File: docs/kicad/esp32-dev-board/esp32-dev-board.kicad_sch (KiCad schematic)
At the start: 6 parts, among them K1 2-Ch Relay Module, U1 ESP32 Dev Board, U2 DS18B20 Solar, U3 DS18B20 Pool

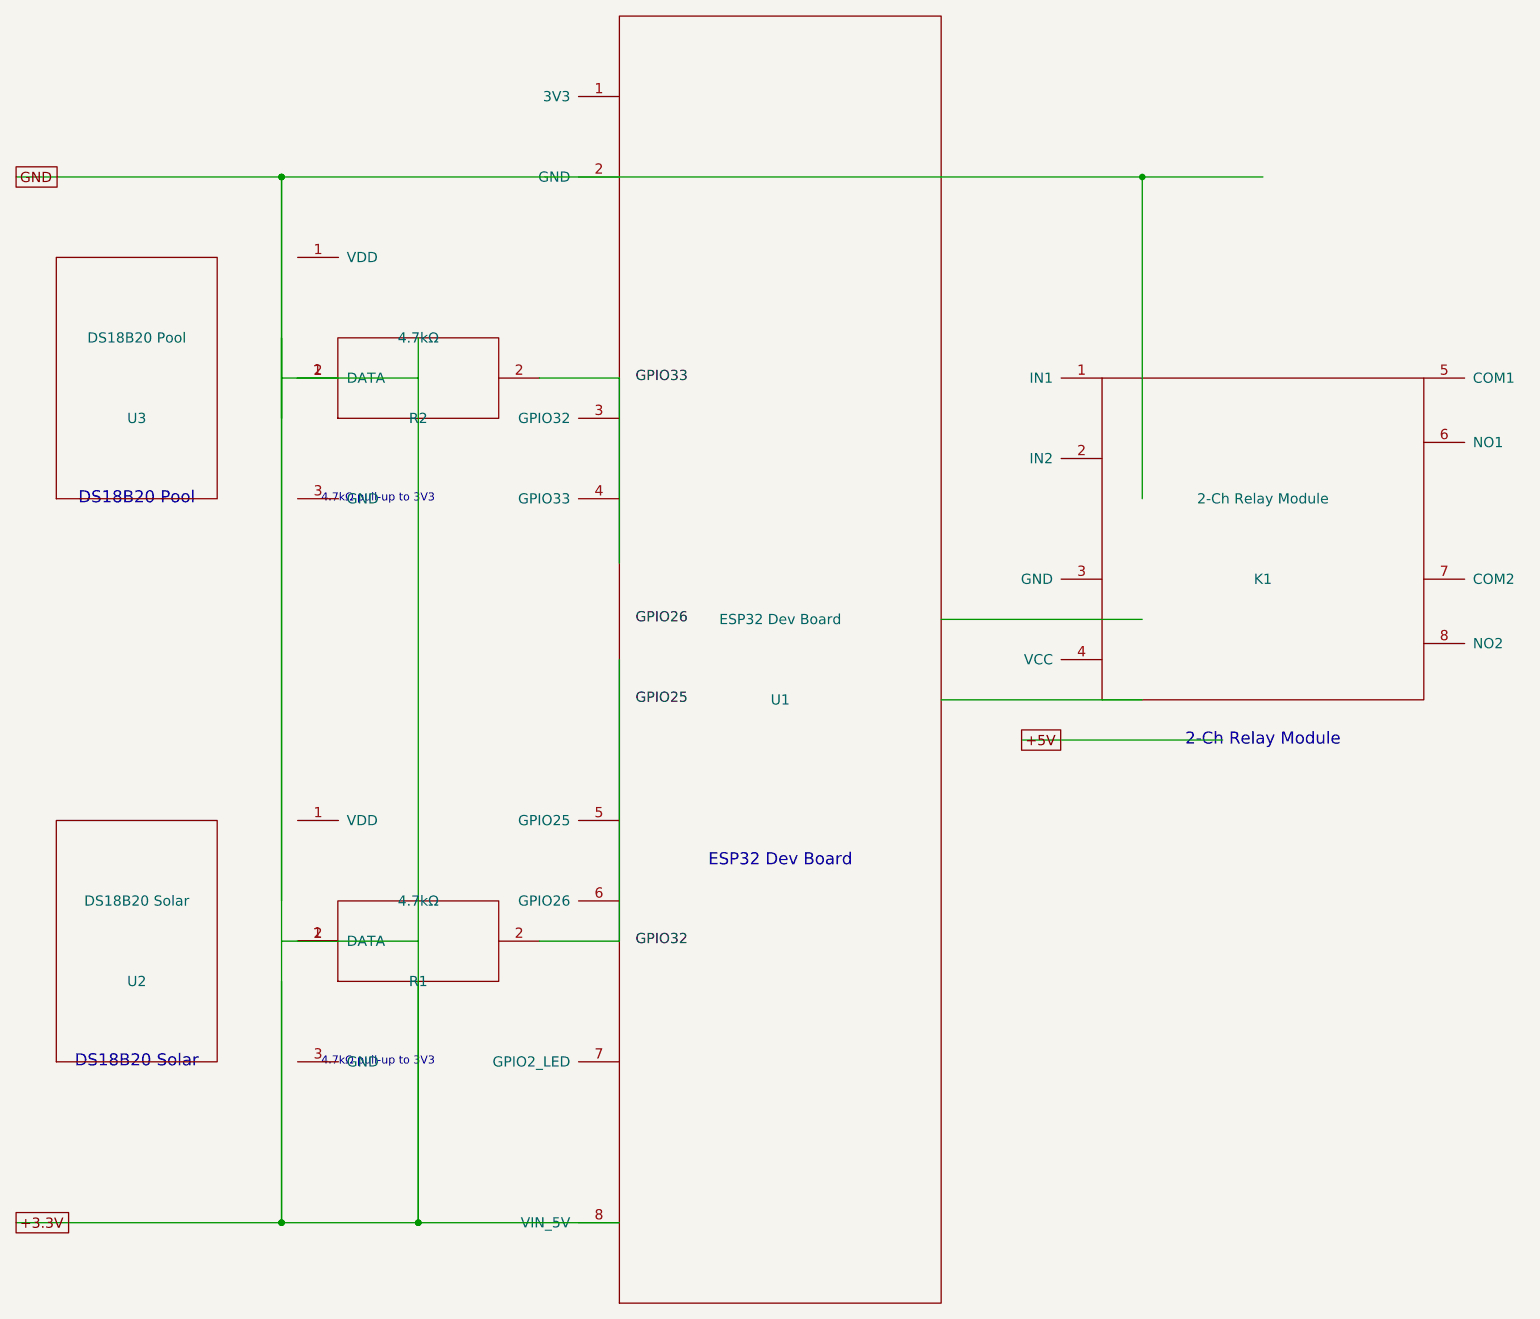
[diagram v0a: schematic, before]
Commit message: fix: review comments and Super-Linter quality gate failures
- docs/hardware-guide.md: fix MD012 (double blank line) and MD013 (line too long at 143 chars → 111)
- src/OtaUpdater.cpp: replace ISRG Root X1 with DigiCert Global Root G2 for GitHub release download endpoints
- scripts/gen-kicad-sch.py: fix KiCad pin coordinate system (y_abs = y_inst − py, not +); use power symbols on supply pins, vertical pull-up resistors (rot=90), and net labels for signals so KiCad nets are electrically correct
- docs/kicad/*/: regenerate .kicad_sch files from corrected generator
- remove stale esp32-dev-board-erc.rpt and norvi-ae01-r-erc.rpt from repo root
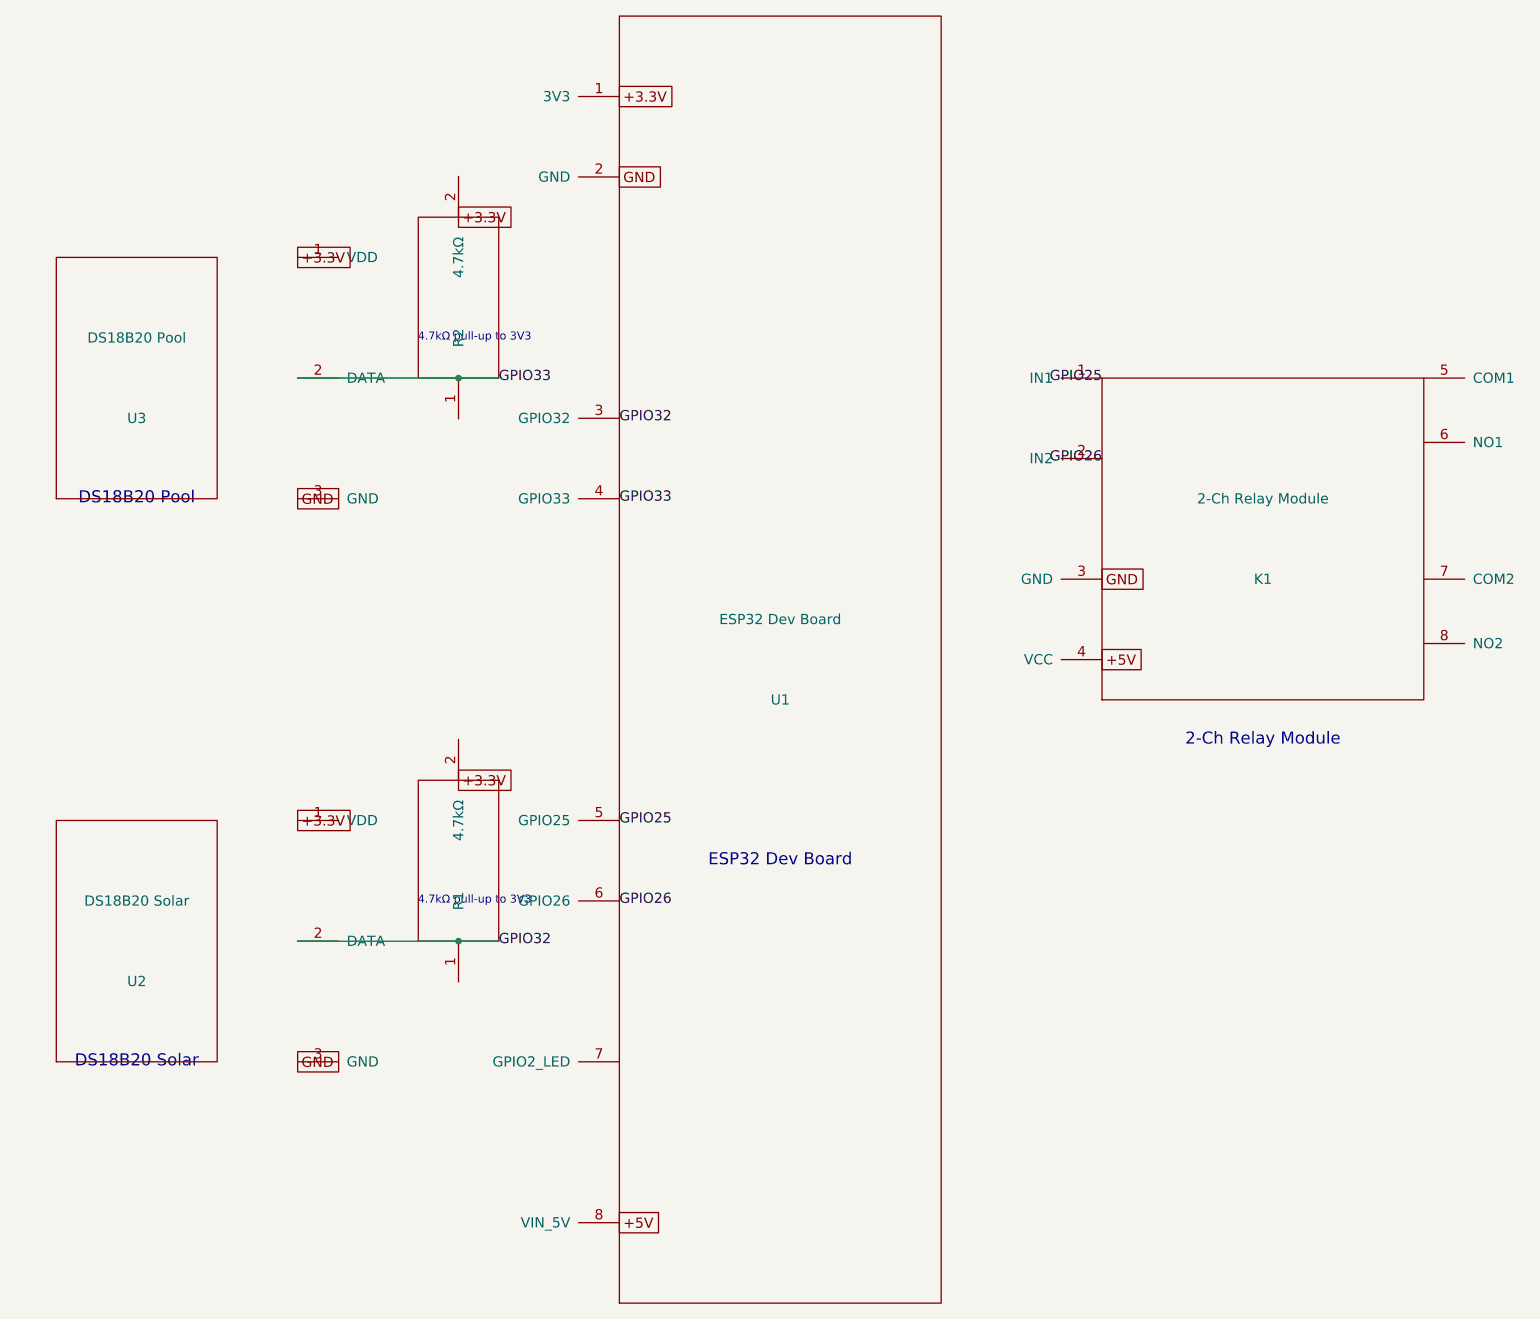
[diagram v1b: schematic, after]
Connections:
- net +3.3V: now also R1.2, R2.2, U1.1 (3V3), U2.1 (VDD), U3.1 (VDD); no longer U1.8 (VIN_5V)
- net +5V: now also K1.4 (VCC), U1.8 (VIN_5V)
- net GPIO25: now also K1.1 (IN1), U1.5 (GPIO25)
- net GPIO26: now also K1.2 (IN2), U1.6 (GPIO26)
- net GPIO32: now also R1.1, U1.3 (GPIO32), U2.2 (DATA)
- net GPIO33: now also R2.1, U1.4 (GPIO33), U3.2 (DATA)
- net GND: now reaches U2.3 (GND)
- net GND: now also K1.3 (GND), U1.2 (GND), U3.3 (GND)
